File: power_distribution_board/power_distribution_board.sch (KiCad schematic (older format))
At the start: 65 parts

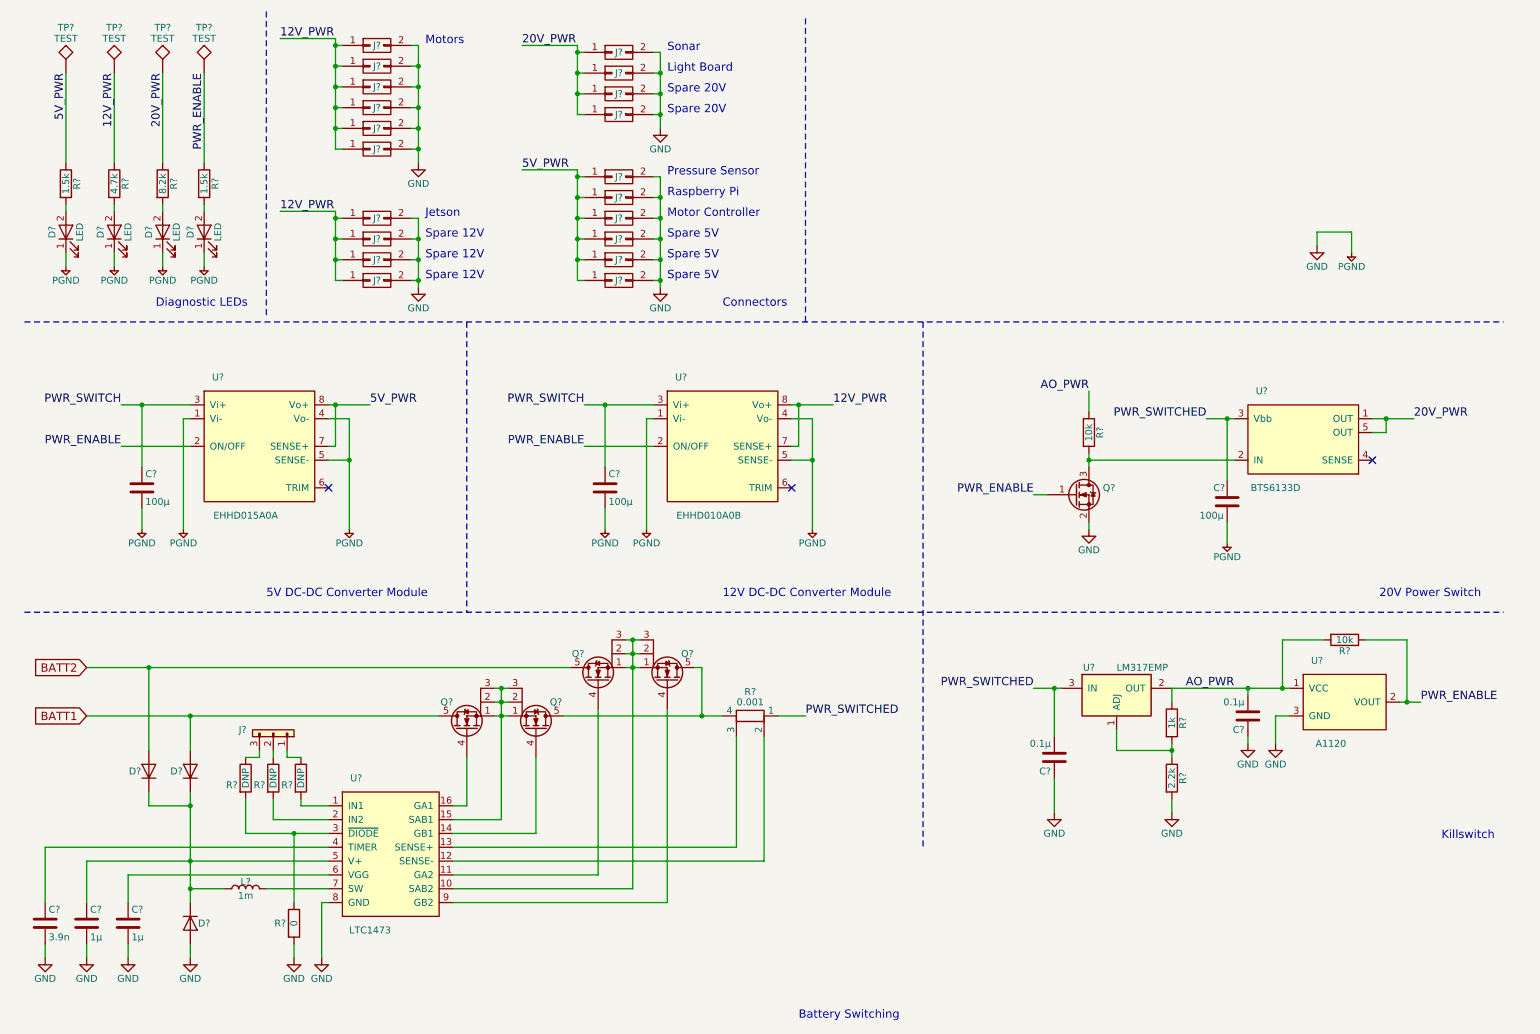
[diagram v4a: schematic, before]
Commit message: annotate and fix warnings/errors
Added:
- Power flags
- Battery connectors
Fixed:
- Incorrect net names
'Fixed':
- Change Vo- of DC-DC converters to be passive, so they can be connected
  each other via ground.
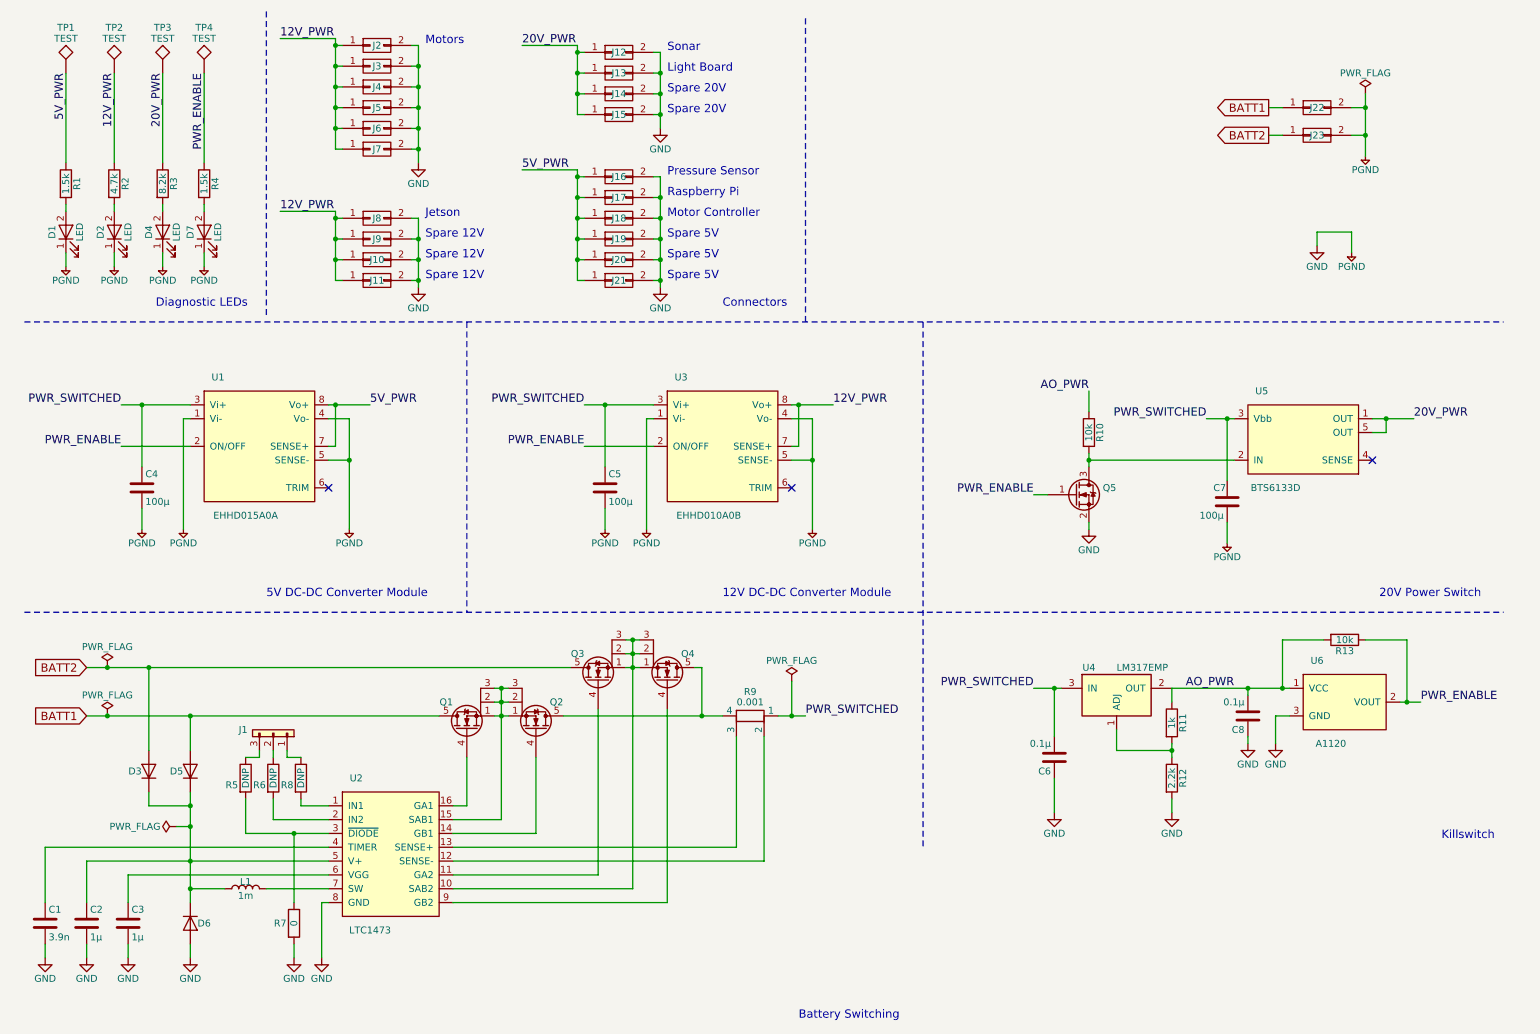
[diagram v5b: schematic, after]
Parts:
- added J22, J23: CONN_02X01, symbol CONN_02X01
- gave numbers to parts that had none: 65
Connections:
- net PWR_SWITCH is gone; now on net PWR_SWITCHED: C4.1, C5.1, U1.3 (Vi+), U3.3 (Vi+)
- net BATT1: now also J22.1 (P1)
- net BATT2: now also J23.1 (P1)
- net GND: now also J22.2 (P2), J23.2 (P2)

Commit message: add custom footprints
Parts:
- R1, R10, R11, R12, R13, R2, R3, R4, R5, R6, R7, R8, R9: footprint (none) -> Resistors_SMD:R_0603
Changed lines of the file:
@@
 F 0 "R9" V 5575 5550 50  0000 C CNN
 F 1 "0.001" V 5650 5550 50  0000 C CNN
-F 2 "" V 5680 5550 50  0001 C CNN
+F 2 "Resistors_SMD:R_0603" V 5680 5550 50  0001 C CNN
 F 3 "" H 5750 5550 50  0001 C CNN
 	1    5750 5550
@@
 F 0 "R6" H 2200 5950 50  0000 C CNN
 F 1 "DNP" V 2300 6000 50  0000 C CNN
-F 2 "" V 2230 6000 50  0001 C CNN
+F 2 "Resistors_SMD:R_0603" V 2230 6000 50  0001 C CNN
 F 3 "" H 2300 6000 50  0001 C CNN
 	1    2300 6000
@@
 F 0 "R8" H 2400 5950 50  0000 C CNN
 F 1 "DNP" V 2500 6000 50  0000 C CNN
-F 2 "" V 2430 6000 50  0001 C CNN
+F 2 "Resistors_SMD:R_0603" V 2430 6000 50  0001 C CNN
 F 3 "" H 2500 6000 50  0001 C CNN
 	1    2500 6000
@@
 F 0 "R7" H 2350 7050 50  0000 C CNN
 F 1 "0" V 2450 7050 50  0000 C CNN
-F 2 "" V 2380 7050 50  0001 C CNN
+F 2 "Resistors_SMD:R_0603" V 2380 7050 50  0001 C CNN
 F 3 "" H 2450 7050 50  0001 C CNN
 	1    2450 7050
@@
 F 0 "R5" H 2000 5950 50  0000 C CNN
 F 1 "DNP" V 2100 6000 50  0000 C CNN
-F 2 "" V 2030 6000 50  0001 C CNN
+F 2 "Resistors_SMD:R_0603" V 2030 6000 50  0001 C CNN
 F 3 "" H 2100 6000 50  0001 C CNN
 	1    2100 6000
@@
 F 0 "R13" V 10130 5000 50  0000 C CNN
 F 1 "10k" V 10050 5000 50  0000 C CNN
-F 2 "" V 9980 5000 50  0001 C CNN
+F 2 "Resistors_SMD:R_0603" V 9980 5000 50  0001 C CNN
 F 3 "" H 10050 5000 50  0001 C CNN
 	1    10050 5000
@@
 F 0 "R11" V 8880 5600 50  0000 C CNN
 F 1 "1k" V 8800 5600 50  0000 C CNN
-F 2 "" V 8730 5600 50  0001 C CNN
+F 2 "Resistors_SMD:R_0603" V 8730 5600 50  0001 C CNN
 F 3 "" H 8800 5600 50  0001 C CNN
 	1    8800 5600
@@
 F 0 "R12" V 8880 6000 50  0000 C CNN
 F 1 "2.2k" V 8800 6000 50  0000 C CNN
-F 2 "" V 8730 6000 50  0001 C CNN
+F 2 "Resistors_SMD:R_0603" V 8730 6000 50  0001 C CNN
 F 3 "" H 8800 6000 50  0001 C CNN
 	1    8800 6000
@@
 F 0 "R10" V 8280 3500 50  0000 C CNN
 F 1 "10k" V 8200 3500 50  0000 C CNN
-F 2 "" V 8130 3500 50  0001 C CNN
+F 2 "Resistors_SMD:R_0603" V 8130 3500 50  0001 C CNN
 F 3 "" H 8200 3500 50  0001 C CNN
 	1    8200 3500
@@
 F 0 "R1" V 880 1700 50  0000 C CNN
 F 1 "1.5k" V 800 1700 50  0000 C CNN
-F 2 "" V 730 1700 50  0001 C CNN
+F 2 "Resistors_SMD:R_0603" V 730 1700 50  0001 C CNN
 F 3 "" H 800 1700 50  0001 C CNN
 	1    800  1700
@@
 F 0 "R2" V 1230 1700 50  0000 C CNN
 F 1 "4.7k" V 1150 1700 50  0000 C CNN
-F 2 "" V 1080 1700 50  0001 C CNN
+F 2 "Resistors_SMD:R_0603" V 1080 1700 50  0001 C CNN
 F 3 "" H 1150 1700 50  0001 C CNN
 	1    1150 1700
@@
 F 0 "R3" V 1580 1700 50  0000 C CNN
 F 1 "8.2k" V 1500 1700 50  0000 C CNN
-F 2 "" V 1430 1700 50  0001 C CNN
+F 2 "Resistors_SMD:R_0603" V 1430 1700 50  0001 C CNN
 F 3 "" H 1500 1700 50  0001 C CNN
 	1    1500 1700
@@
 F 0 "R4" V 1880 1700 50  0000 C CNN
 F 1 "1.5k" V 1800 1700 50  0000 C CNN
-F 2 "" V 1730 1700 50  0001 C CNN
+F 2 "Resistors_SMD:R_0603" V 1730 1700 50  0001 C CNN
 F 3 "" H 1800 1700 50  0001 C CNN
 	1    1800 1700

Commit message: assign footprints
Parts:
- C1, C2, C3, C6, C8: footprint (none) -> Capacitors_SMD:C_0603
- C4, C5, C7: footprint (none) -> Capacitors_SMD:C_1210
- D1, D2, D4, D7: footprint (none) -> LEDs:LED_0805
- D3, D5, D6: footprint (none) -> Diodes_SMD:D_SMA
- J1, U6: footprint (none) -> Connectors_Molex:Molex_KK-6410-03_03x2.54mm_Straight
- J10, J11, J12, J13, J14, J15, J16, J17, J18, J19, J2, J20, J21, J22, J23, J3, J4, J5, J6, J7, J8, J9: footprint (none) -> Connectors_Molex:Molex_MiniFit-JR-5556-02A_2x01x4.20mm_Straight
- L1: footprint (none) -> Inductors_SMD:L_0805
- Q1, Q2, Q3, Q4: footprint (none) -> TO_SOT_Packages_SMD:SOT-669_LFPAK
- Q5: footprint (none) -> TO_SOT_Packages_SMD:SOT-23
- R9: footprint Resistors_SMD:R_0603 -> cauv_lib:WSLP2726
- TP1, TP2, TP3, TP4: footprint (none) -> agg_lib:TESTPAD
- U1, U3: footprint (none) -> cauv_lib:EHHD015A0A
- U5: footprint (none) -> cauv_lib:DSO-12-9

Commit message: Update BTS6133D to have the correct footprint
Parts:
- U5: footprint cauv_lib:DSO-12-9 -> TO_SOT_Packages_SMD:TO-252-5_TabPin3
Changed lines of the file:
@@
 F 0 "U5" H 9450 3800 50  0000 C CNN
 F 1 "BTS6133D" H 9550 3100 50  0000 C CNN
-F 2 "cauv_lib:DSO-12-9" H 10800 3100 50  0001 C CNN
+F 2 "TO_SOT_Packages_SMD:TO-252-5_TabPin3" H 10800 3100 50  0001 C CNN
 F 3 "" H 10800 3100 50  0001 C CNN
 	1    9750 3500
